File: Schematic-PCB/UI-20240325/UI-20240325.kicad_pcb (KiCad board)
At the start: 2 copper layers, 82.9 x 53.9 mm, 21 parts, among them J1 Conn_01x10_Pin

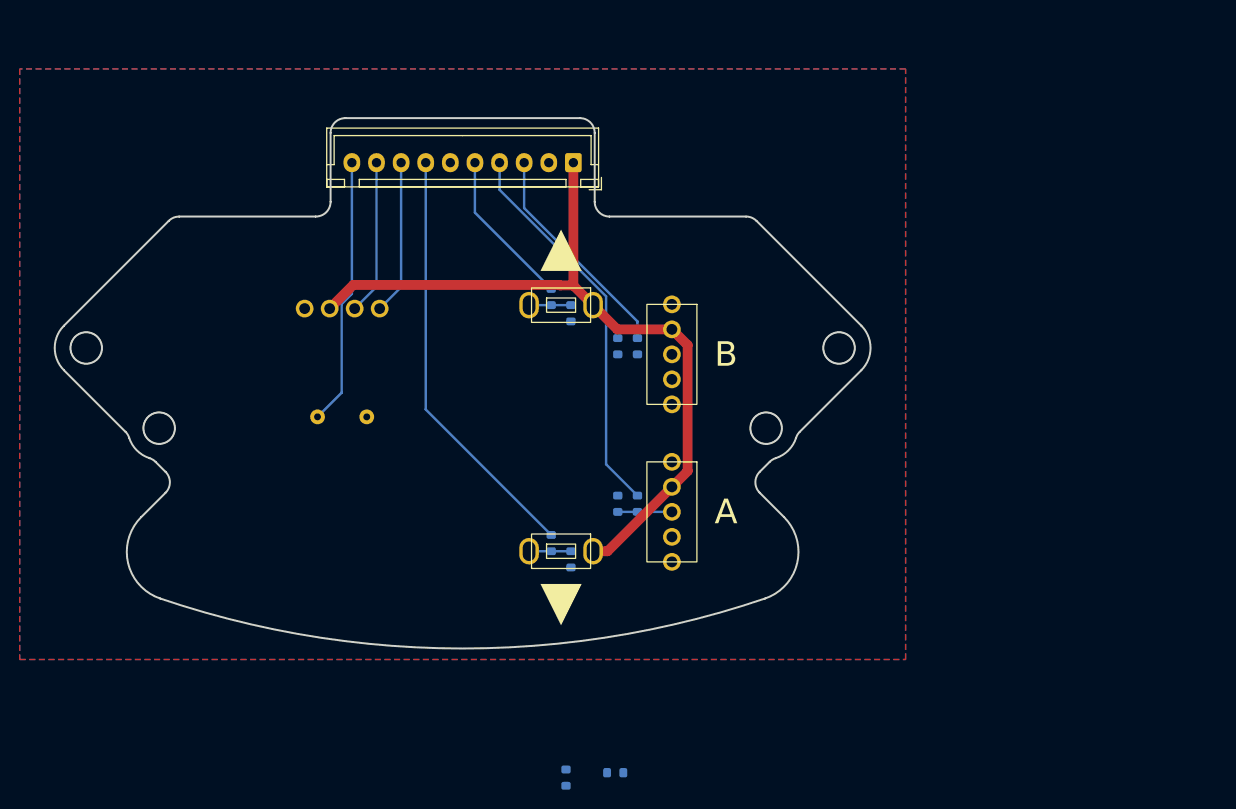
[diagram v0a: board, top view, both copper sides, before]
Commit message: UI基板のPCBを更新しました
DRをお願いします。
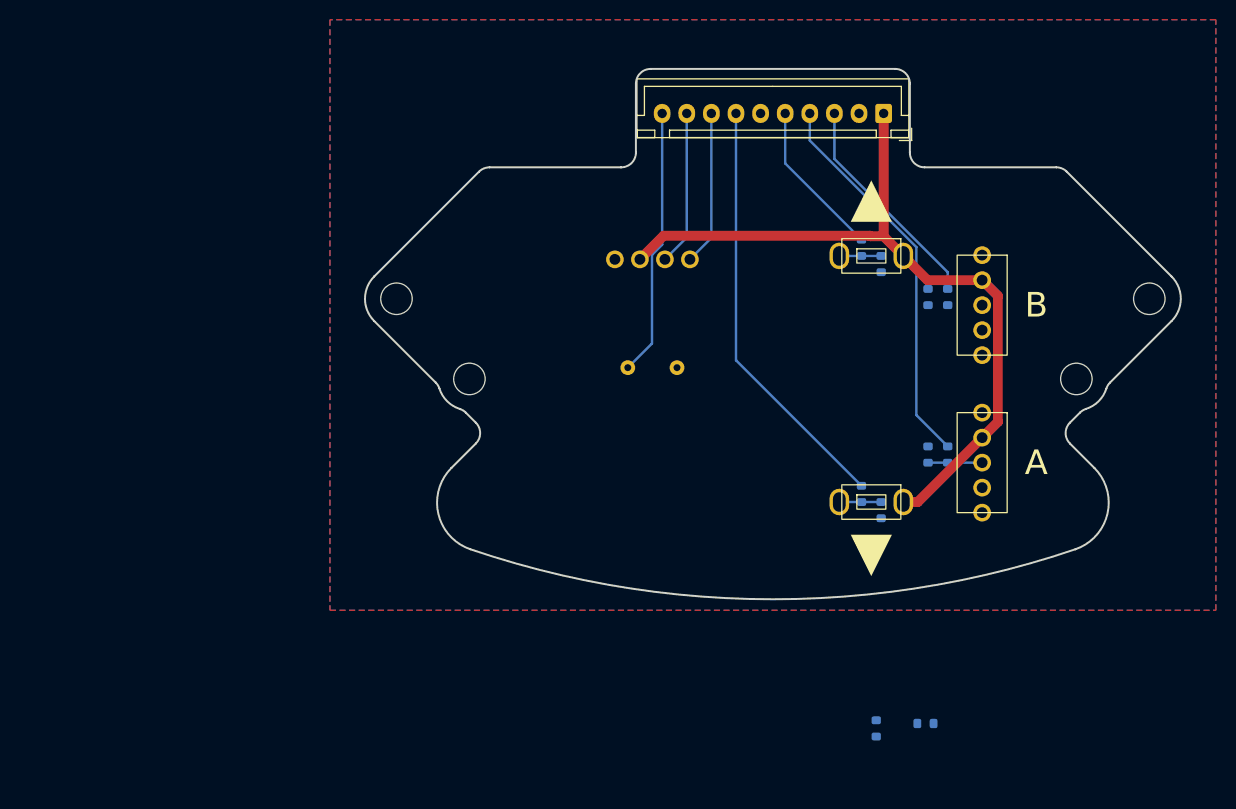
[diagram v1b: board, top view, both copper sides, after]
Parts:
- moved REF** 31.9 mm to (90.9, 83.1)
- moved A 31.9 mm to (143.0, 91.6)
- moved B 31.9 mm to (143.0, 75.6)
- moved BZ1 31.9 mm to (109.5, 82.0)
- moved J1 31.9 mm to (133.0, 56.2)
- moved R1 31.9 mm to (139.5, 74.8)
- moved R10 31.9 mm to (132.8, 96.5)
- moved R2 31.9 mm to (139.5, 90.8)
- moved R3 31.9 mm to (137.5, 74.8)
- moved R4 31.9 mm to (137.5, 90.8)
- moved R5 31.9 mm to (130.8, 69.8)
- moved R6 31.9 mm to (137.3, 118.1)
- moved R7 31.9 mm to (130.8, 94.8)
- moved R8 31.9 mm to (132.8, 71.5)
- moved R9 31.9 mm to (132.3, 118.6)
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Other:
- outline, holes or cut-outs redrawn

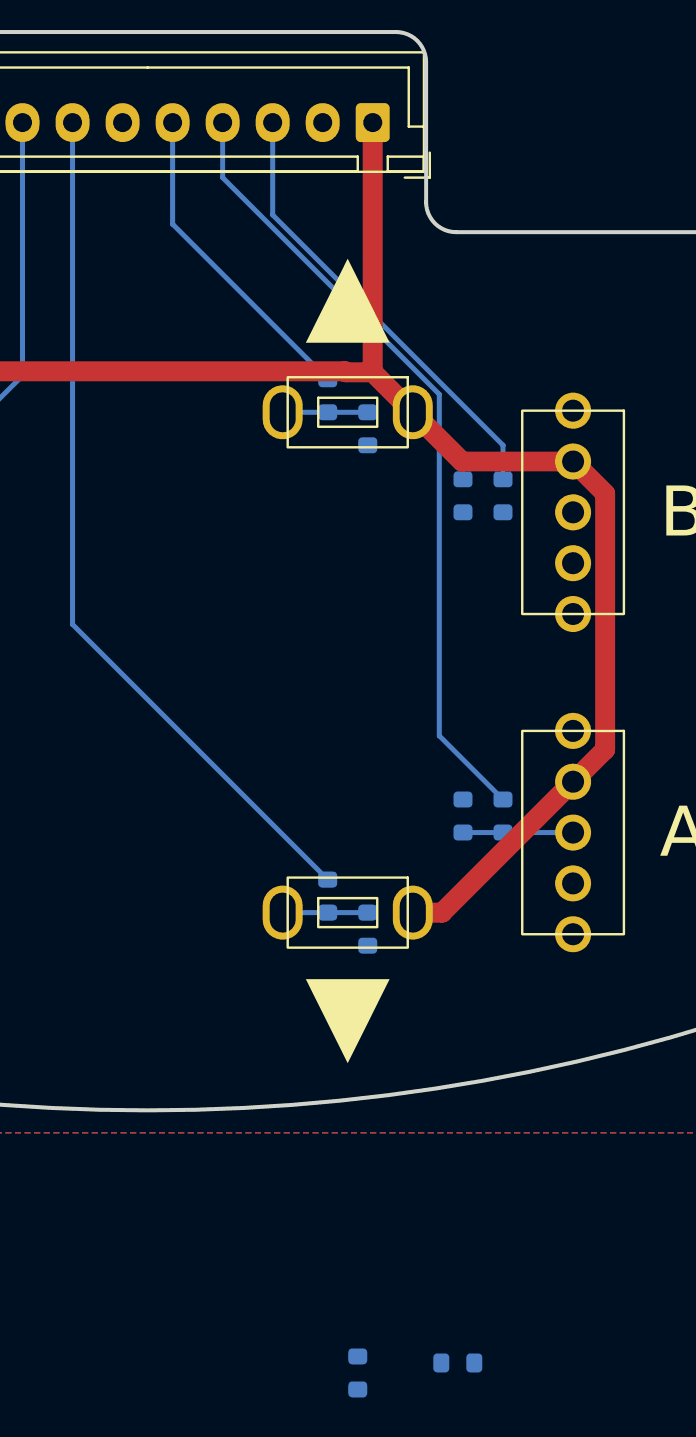
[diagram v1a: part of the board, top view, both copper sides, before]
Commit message: Ui基板の回路図・PCBデザインを更新しました
DR & 修正・SW-4に関する変更
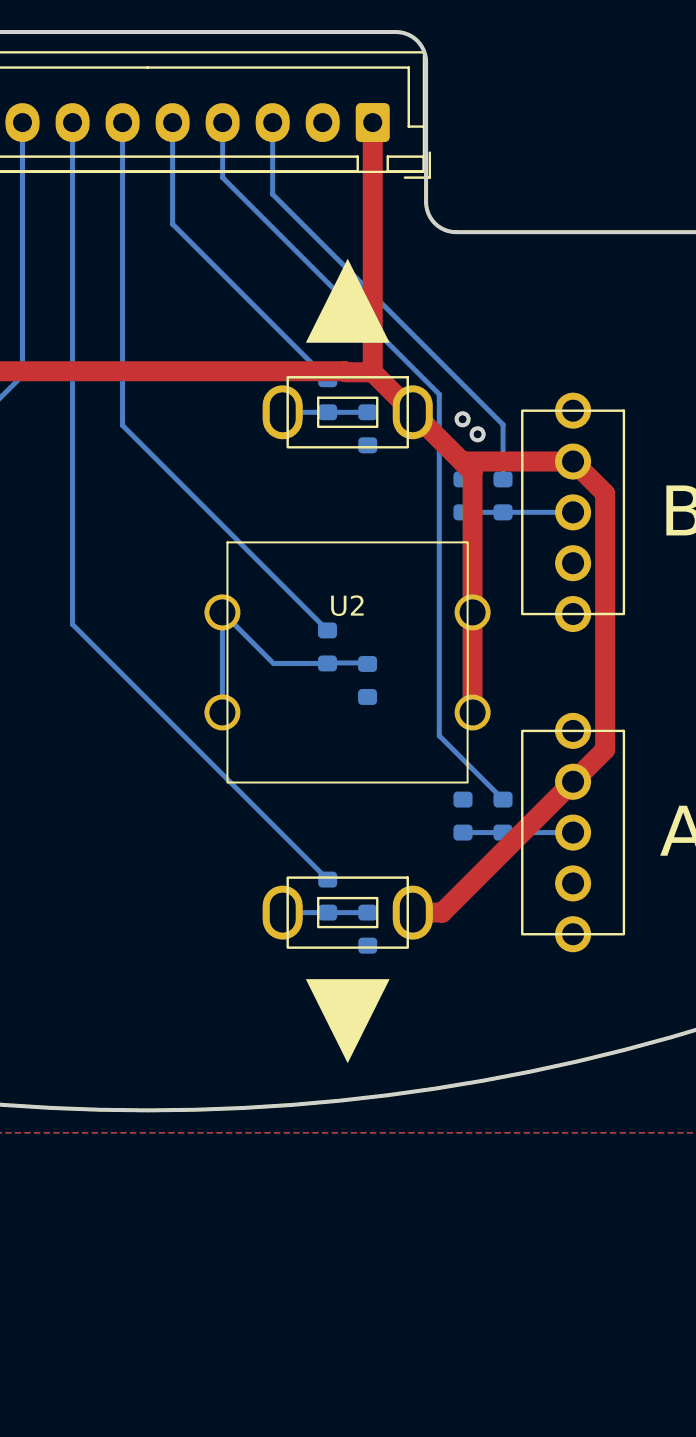
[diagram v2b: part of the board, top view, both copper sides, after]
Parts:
- added U2: ~, @2024-UI:TVGP01-G73BB, F.Cu at (131.8, 83.2)
- moved R6 36.4 mm to (130.8, 82.4), turned to -90 degrees
- moved R9 34.6 mm to (132.8, 84.0), turned to 90 degrees
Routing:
- net SW-TAC-2: track 0.00 -> 29.6 mm
- net Net-(R6-Pad2): track 0.00 -> 13.3 mm
- net +3.3V: track 78.2 -> 90.9 mm
- net Net-(SW1-B): track 0.00 -> 5.50 mm
- net GND: vias 0 -> 2

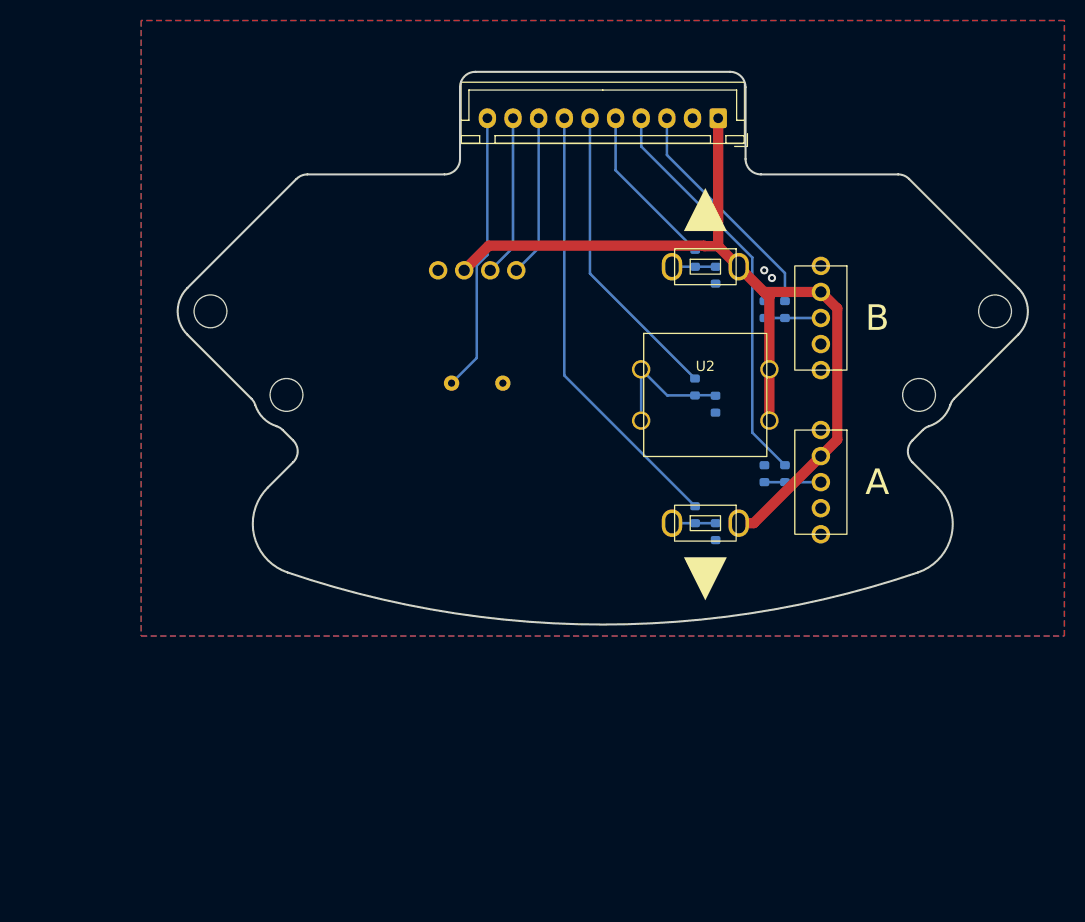
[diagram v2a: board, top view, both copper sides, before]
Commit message: UI基板の回路図とPCBを作成しなおした
DRよろしく
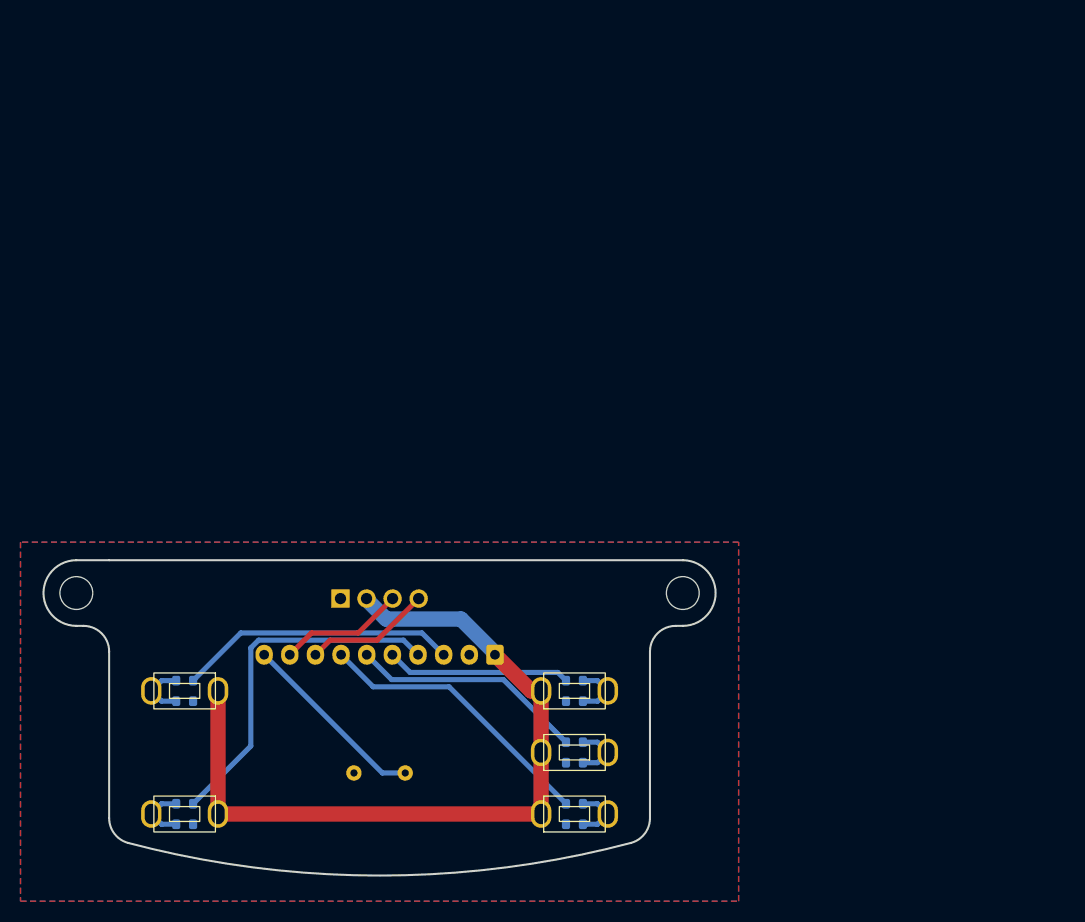
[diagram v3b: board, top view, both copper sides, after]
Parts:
- removed A, B: SW_SPDT, @2024-UI:2MS1-T1-B4-VS2-Q-E-S
- removed the REF** at (90.9, 83.1)
- removed the REF** at (152.6, 83.1)
- removed the REF** at (83.5, 75.0)
- removed the REF** at (160.0, 75.0)
- removed U2: ~, @2024-UI:TVGP01-G73BB
- removed ▲, ▼: SW_Push, @2024-UI:TVBP06-B043C
- added REF**: MountingHole_3.2mm_M3, MountingHole:MountingHole_3.2mm_M3, F.Cu at (129.6, 102.5)
- added REF**: MountingHole_3.2mm_M3, MountingHole:MountingHole_3.2mm_M3, F.Cu at (70.4, 102.5)
- added SW1: SW_Push, @2024-UI:TVBP06-B043C, F.Cu at (81.0, 112.0)
- added SW2: SW_Push, @2024-UI:TVBP06-B043C, F.Cu at (81.0, 124.0)
- added SW3: SW_Push, @2024-UI:TVBP06-B043C, F.Cu at (119.0, 112.0)
- added SW4: SW_Push, @2024-UI:TVBP06-B043C, F.Cu at (119.0, 118.0)
- added SW5: SW_Push, @2024-UI:TVBP06-B043C, F.Cu at (119.0, 124.0)
- J1: moved to B.Cu
- R3, R4: value 10K -> 1K
- R6, R7: value 1K -> 10K
- moved R1 68.8 mm to (81.0, 111.0), turned to 180 degrees
- moved R2 66.8 mm to (81.0, 123.0), turned to 180 degrees
- moved R6 58.4 mm to (81.0, 113.0), turned to 180 degrees
- moved R7 58.2 mm to (81.0, 125.0), turned to 180 degrees
- moved J1 56.6 mm to (111.2, 108.5)
- moved R5 54.5 mm to (119.0, 123.0), turned to 0 degrees
- moved R8 43.7 mm to (119.0, 113.0), turned to 0 degrees
- moved R3 40.6 mm to (119.0, 111.0), turned to 0 degrees
- moved BZ1 39.2 mm to (100.0, 120.0), turned to 180 degrees
- moved R9 37.6 mm to (119.0, 119.0), turned to 0 degrees
- moved U1 33.4 mm to (100.0, 103.0)
- moved R4 32.1 mm to (119.0, 117.0), turned to 0 degrees
- moved R10 31.7 mm to (119.0, 125.0), turned to 0 degrees
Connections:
- J1 pad 3: SW-TOG-1 -> SW-TAC-1
- J1 pad 4: SW-TOG-2 -> SW-TAC-2
- J1 pad 5: SW-TAC-1 -> SW-TAC-3
- J1 pad 6: SW-TAC-2 -> SW-TAC-4
- J1 pad 7: SW-TAC-3 -> SW-TAC-5
- R1 pad 1: SW-TOG-1 -> SW-TAC-1
- R1 pad 2: Net-(SW1-B) -> Net-(R1-Pad2)
- R2 pad 1: SW-TOG-2 -> SW-TAC-2
- R2 pad 2: Net-(SW2-B) -> Net-(R2-Pad2)
- R3 pad 1: GND -> SW-TAC-3
- R3 pad 2: Net-(SW1-B) -> Net-(R3-Pad2)
- R4 pad 1: GND -> SW-TAC-4
- R4 pad 2: Net-(SW2-B) -> Net-(R4-Pad2)
- R5 pad 1: SW-TAC-1 -> SW-TAC-5
- R5 pad 2: Net-(R5-Pad2) -> Net-(R10-Pad2)
- R6 pad 1: SW-TAC-2 -> GND
- R6 pad 2: Net-(R6-Pad2) -> Net-(R1-Pad2)
- R7 pad 1: SW-TAC-3 -> GND
- R7 pad 2: Net-(R10-Pad2) -> Net-(R2-Pad2)
- R8 pad 2: Net-(R5-Pad2) -> Net-(R3-Pad2)
- R9 pad 2: Net-(R6-Pad2) -> Net-(R4-Pad2)
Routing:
- net SW-TOG-2: track 39.6 -> 0.00 mm
- net SW-TAC-5: track 0.00 -> 27.9 mm
- net SW-TAC-3: track 43.1 -> 18.0 mm
- net SW-TAC-4: track 0.00 -> 23.0 mm
- net SW-TOG-1: track 22.6 -> 0.00 mm
- net +3.3V: track 90.9 -> 76.4 mm
- net Net-(R6-Pad2): track 13.3 -> 0.00 mm
- net SW-TAC-1: track 16.0 -> 27.2 mm
- net BUZZER: track 27.3 -> 18.5 mm
- net Net-(R4-Pad2): track 0.00 -> 5.68 mm
- net Net-(R3-Pad2): track 0.00 -> 5.68 mm
- net Net-(R2-Pad2): track 0.00 -> 5.68 mm
- net Net-(R1-Pad2): track 0.00 -> 5.68 mm
- net Net-(SW2-B): track 5.50 -> 0.00 mm
- net Net-(SW1-B): track 5.50 -> 0.00 mm
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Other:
- board size 82.9 x 53.9 mm -> 65.5 x 30.7 mm
